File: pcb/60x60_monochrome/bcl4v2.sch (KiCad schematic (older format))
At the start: 29 parts, among them Q1 BSS138, SW1 SW_Push, SW2 SW_Push, SW3 SW_Push, U1 DS9166A-23, U2 STM32F070CBTx, Y1 Resonator

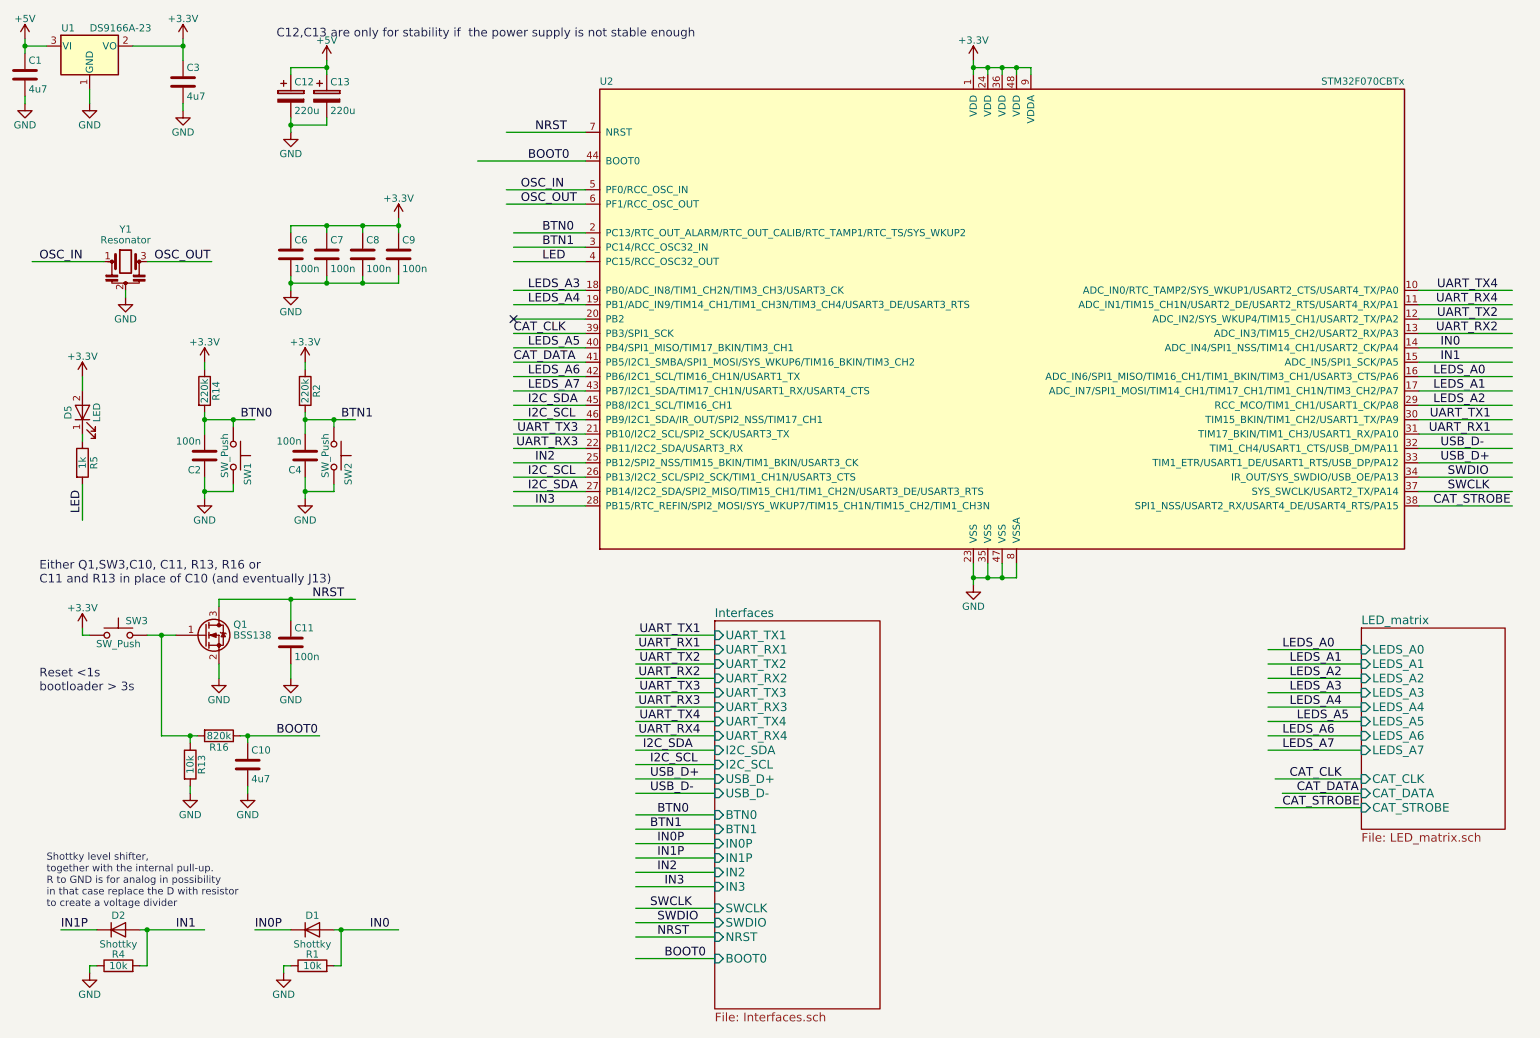
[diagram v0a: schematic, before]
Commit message: - fix some footprints to reduce ERC errors
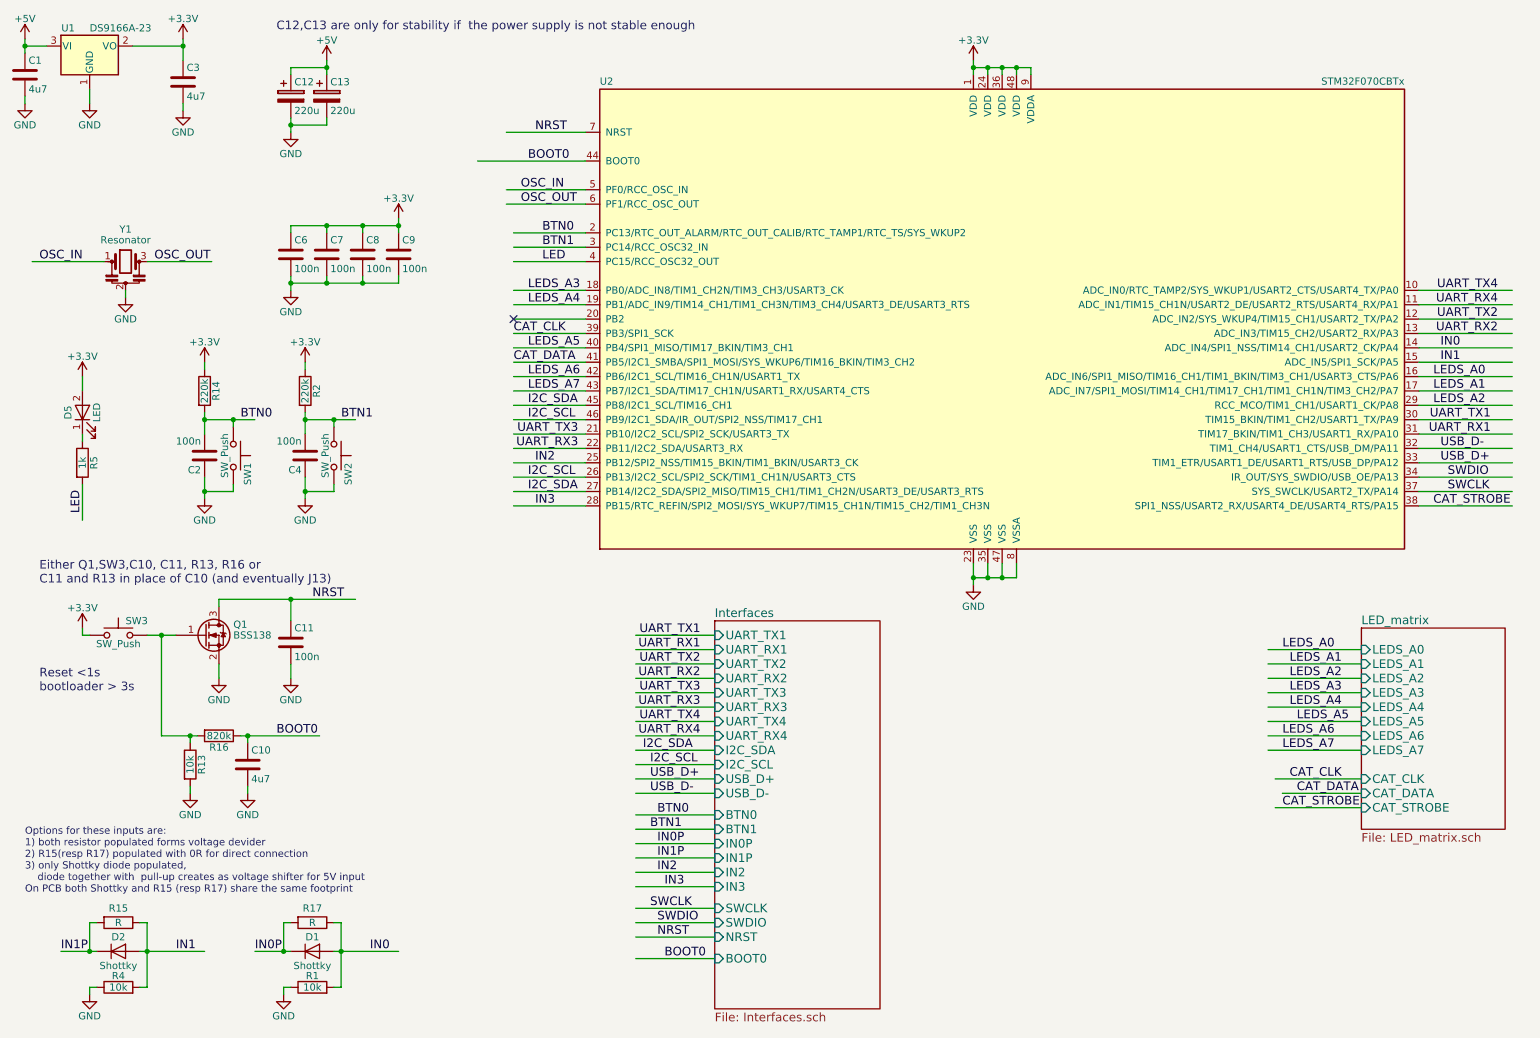
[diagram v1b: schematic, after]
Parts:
- added R15, R17: R, Resistors_SMD:R_0805_HandSoldering, symbol R
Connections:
- wire segments 153 -> 159
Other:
- note added: "Options for these inputs are:\n1) both resistor populated forms voltage devider\n2) R15(resp R17) populated with 0R for direct connection\n3) only Shottky diode populated, \n diode together with pull-up creates as voltage shifter for 5V input\nOn PCB both Shottky and R15 (resp R17) share the same footprint\n"
- note removed: "Shottky level shifter,\ntogether with the internal pull-up.\nR to GND is for analog in possibility\nin that case replace the D with resistor\nto create a voltage divider\n"
- moved on the sheet: D1, D2, R1, R4
